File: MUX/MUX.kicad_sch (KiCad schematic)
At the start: 104 parts, among them P1 Conn_02x36_Top_Bottom, P2 DB9_Male, P3 DB9_Male, P4 DB9_Male, P5 DB9_Male

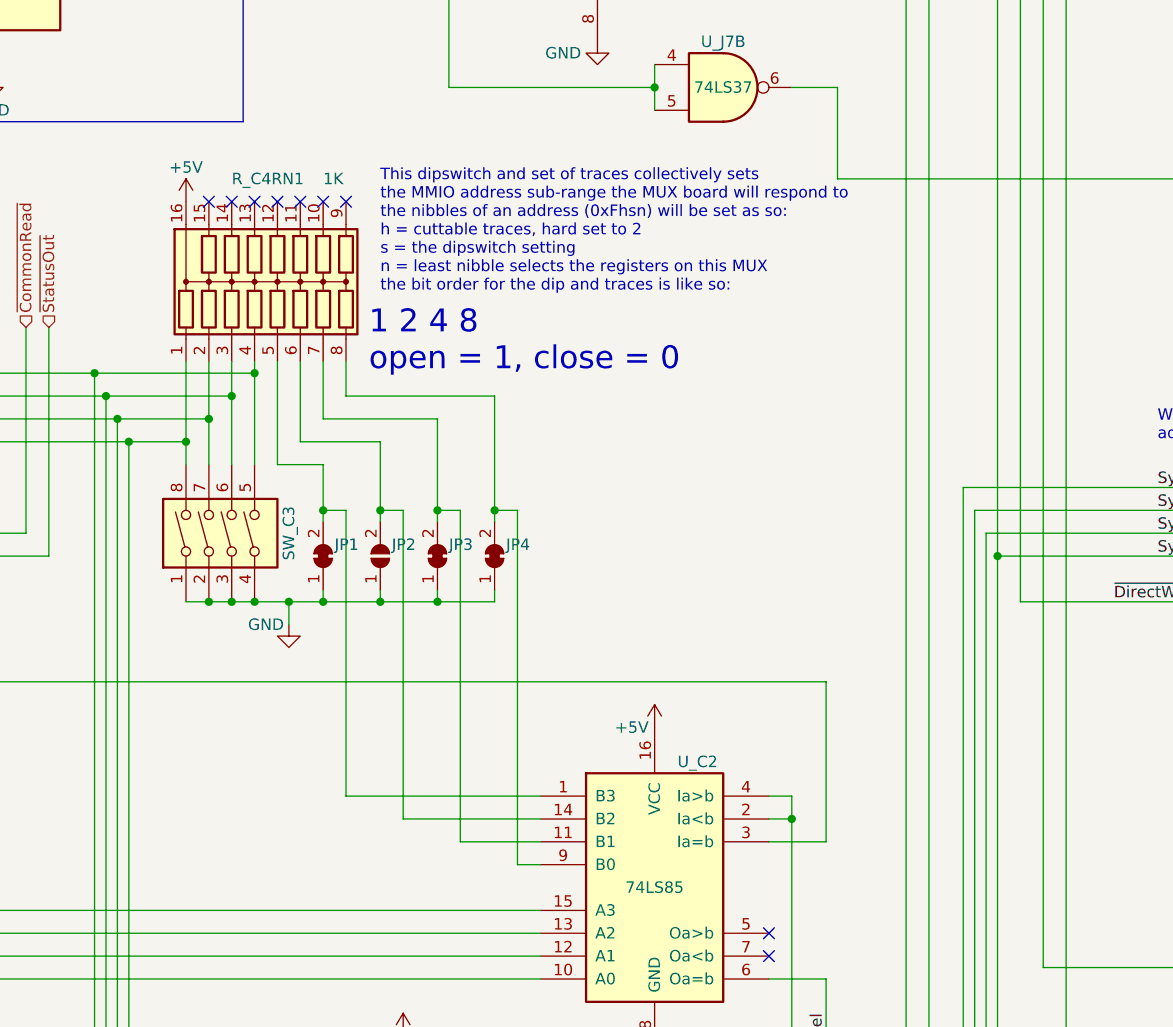
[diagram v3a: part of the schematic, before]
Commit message: Use 8-way DIP switch
Let's not bother with upper half. It's always possible to install a smaller
switch and hard-solder the upper half.
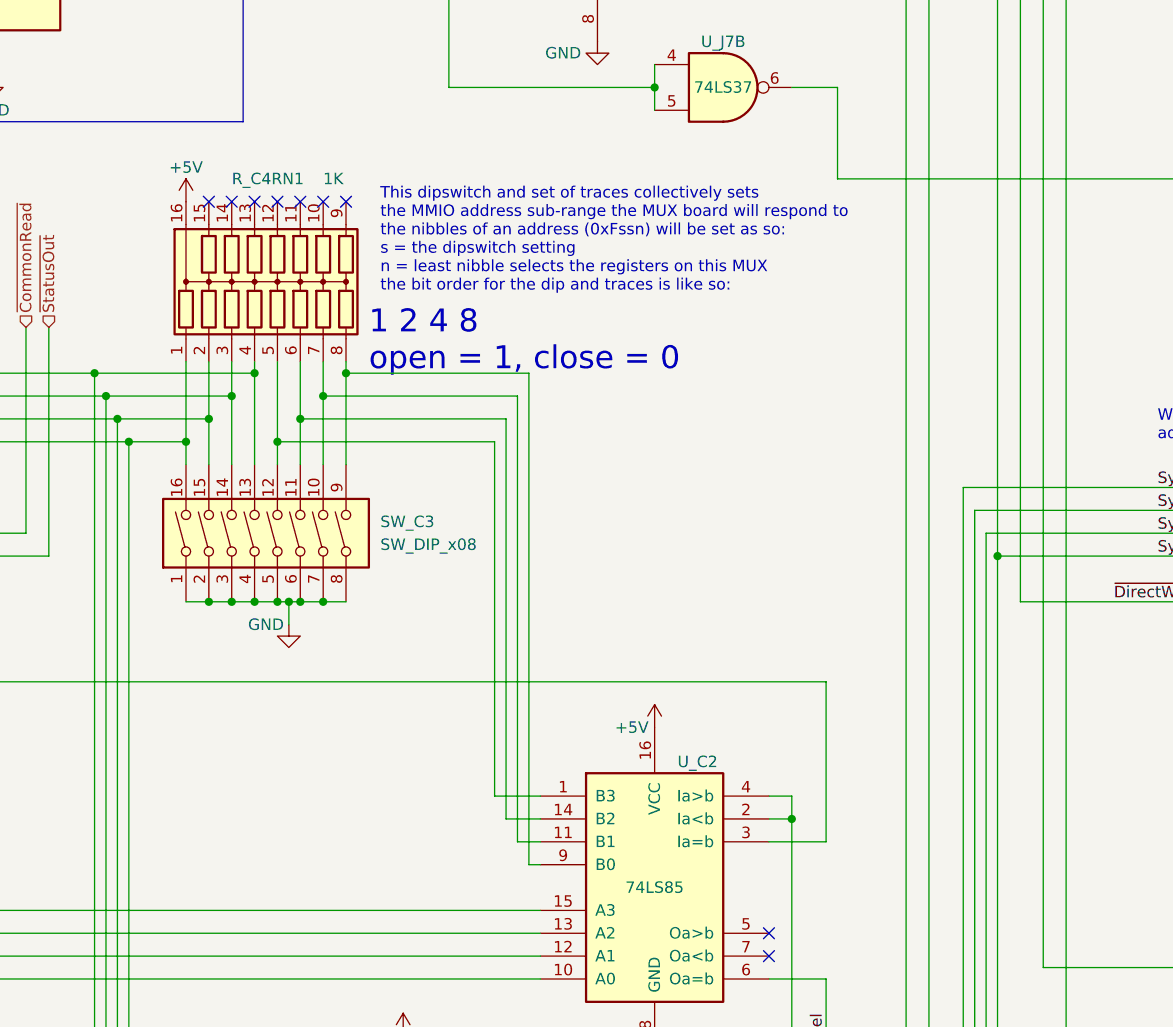
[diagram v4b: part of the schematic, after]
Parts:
- removed JP1, JP3, JP4: SolderJumper_2_Bridged, Connector_PinHeader_2.54mm:PinHeader_1x02_P2.54mm_Vertical, symbol Jumper:SolderJumper_2_Bridged
- removed JP2: SolderJumper_2_Open, Connector_PinHeader_2.54mm:PinHeader_1x02_P2.54mm_Vertical, symbol Jumper:SolderJumper_2_Open
- removed SW_C3: SW_DIP_x04, Button_Switch_THT:SW_DIP_SPSTx04_Slide_6.7x11.72mm_W7.62mm_P2.54mm_LowProfile, symbol Switch:SW_DIP_x04
- added SW_C3: SW_DIP_x08, Button_Switch_THT:SW_DIP_SPSTx08_Slide_6.7x21.88mm_W7.62mm_P2.54mm_LowProfile, symbol Switch:SW_DIP_x08
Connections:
- net GND: now also SW_C3.1, SW_C3.2, SW_C3.3, SW_C3.4, SW_C3.5, SW_C3.6, SW_C3.7, SW_C3.8
- net at R_C4RN1.4, U_C1.9 (B0), U_D4.2 (I1): now also SW_C3.13
- net at R_C4RN1.3, U_C1.11 (B1), U_D4.4 (I2): now also SW_C3.14
- net at R_C4RN1.2, U_C1.14 (B2), U_D4.6 (I3): now also SW_C3.15
- net at R_C4RN1.1, U_C1.1 (B3), U_D4.10 (I4): now also SW_C3.16
- net at R_C4RN1.7, U_C2.11 (B1): now also SW_C3.10
- net at R_C4RN1.6, U_C2.14 (B2): now also SW_C3.11
- net at R_C4RN1.5, U_C2.1 (B3): now also SW_C3.12
- net at R_C4RN1.8, U_C2.9 (B0): now also SW_C3.9
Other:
- note added: "This dipswitch and set of traces collectively sets the MMIO address sub-range the MUX board will respond to the nibbles of an address (0xFssn) will be set as so: s = the dipswitch setting n = least nibble selects the registers on this MUX the bit order for the dip and traces is like so:"
- note removed: "This dipswitch and set of traces collectively sets the MMIO address sub-range the MUX board will respond to the nibbles of an address (0xFhsn) will be set as so: h = cuttable traces, hard set to 2 s = the dipswitch setting n = least nibble selects the registers on this MUX the bit order for the dip and traces is like so:"

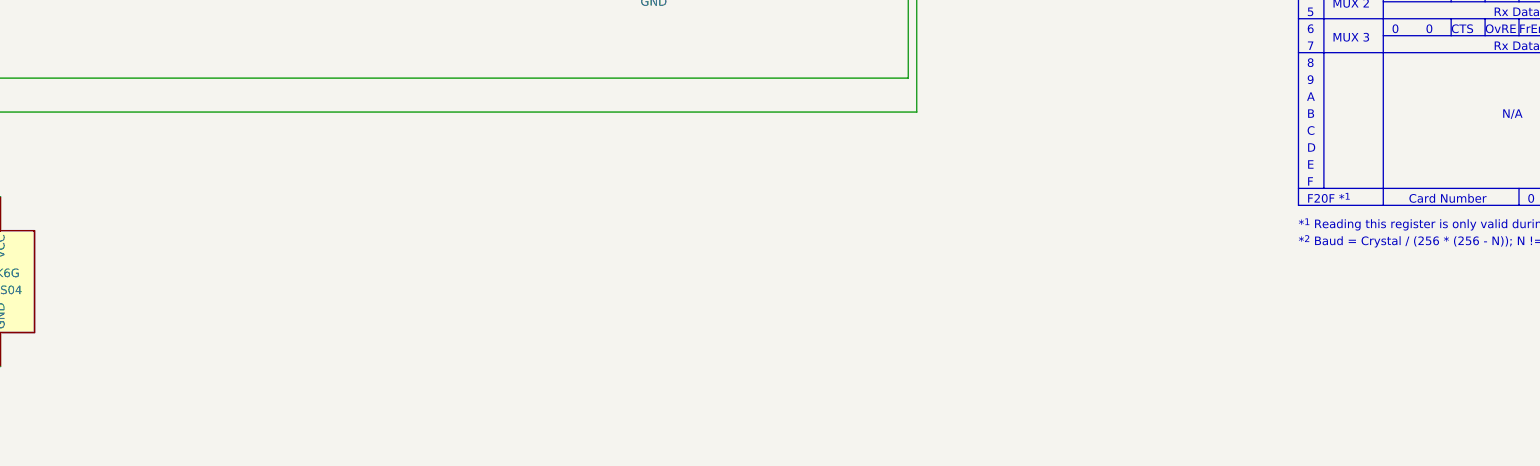
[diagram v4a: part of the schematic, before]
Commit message: MUX: Add decoupling capacitors
Based on the high-res photo. Capacitance values may not be precise, just picked
up reasonable values, like in CPU
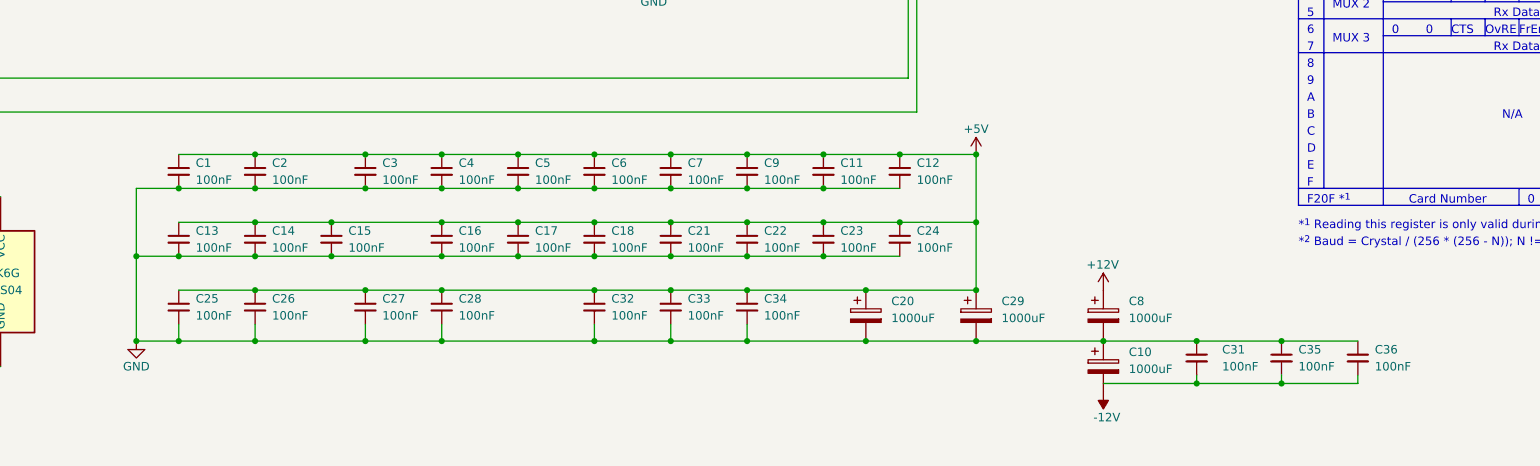
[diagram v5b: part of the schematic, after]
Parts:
- added C1, C11, C12, C13, C14, C15, C16, C17, C18, C2, C21, C22, C23, C24, C25, C26, C27, C28, C3, C31, C32, C33, C34, C35, C36, C4, C5, C6, C7, C9: 100nF, Capacitor_THT:C_Disc_D4.3mm_W1.9mm_P5.00mm, symbol Device:C_Small
- added C10, C20, C29, C8: 1000uF, Capacitor_THT:CP_Radial_D8.0mm_P3.50mm, symbol Device:C_Polarized
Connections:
- net +12V: now also C8.1
- net +5V: now also C1.1, C11.1, C12.1, C13.1, C14.1, C15.1, C16.1, C17.1, C18.1, C2.1, C20.1, C21.1, C22.1, C23.1, C24.1, C25.1, C26.1, C27.1, C28.1, C29.1, C3.1, C32.1, C33.1, C34.1, C4.1, C5.1, C6.1, C7.1, C9.1
- net -12V: now also C10.2
- net GND: now also C1.2, C10.1, C11.2, C12.2, C13.2, C14.2, C15.2, C16.2, C17.2, C18.2, C2.2, C20.2, C21.2, C22.2, C23.2, C24.2, C25.2, C26.2, C27.2, C28.2, C29.2, C3.2, C31.1, C32.2, C33.2, C34.2, C35.1, C36.1, C4.2, C5.2, C6.2, C7.2, C8.2, C9.2
- new net: C31.2, C35.2, C36.2

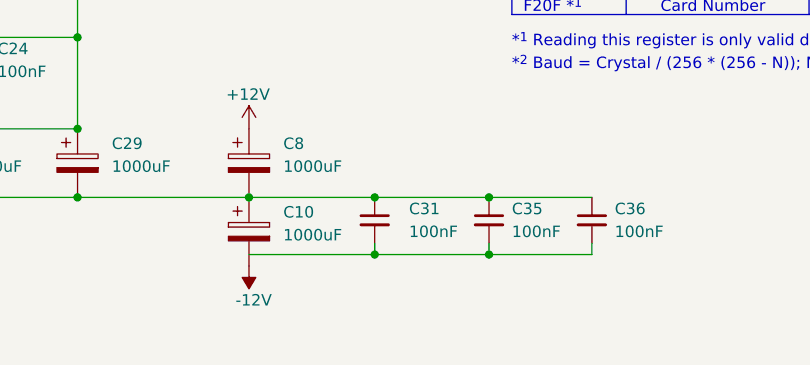
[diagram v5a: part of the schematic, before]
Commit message: MUX: Some schematic fixes
- Proper U_K5 footprint
- Fix 12V filter caps connection
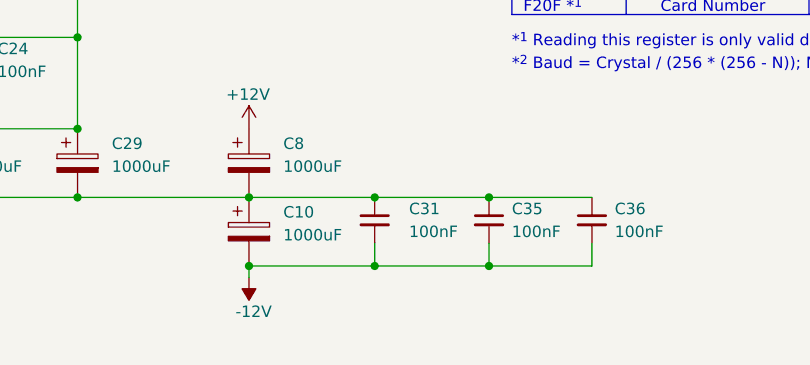
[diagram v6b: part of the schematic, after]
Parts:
- U_K5: footprint Package_DIP:DIP-16_W7.62mm -> Package_DIP:DIP-14_W7.62mm
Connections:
- net -12V: now also C31.2, C35.2, C36.2
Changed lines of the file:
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@@
   (junction (at 788.67 471.17) (diameter 0) (color 0 0 0 0)
   )
+  (junction (at 845.82 496.57) (diameter 0) (color 0 0 0 0)
+  )
   (junction (at 66.04 185.42) (diameter 0) (color 0 0 0 0)
   )
@@
   (junction (at 485.14 467.36) (diameter 0) (color 0 0 0 0)
   )
-  (junction (at 845.82 495.3) (diameter 0) (color 0 0 0 0)
-  )
   (junction (at 388.62 492.76) (diameter 0) (color 0 0 0 0)
   )
@@
   (junction (at 551.18 467.36) (diameter 0) (color 0 0 0 0)
   )
-  (junction (at 833.12 495.3) (diameter 0) (color 0 0 0 0)
-  )
   (junction (at 800.1 488.95) (diameter 0) (color 0 0 0 0)
   )
@@
   (junction (at 755.65 273.05) (diameter 0) (color 0 0 0 0)
   )
+  (junction (at 833.12 496.57) (diameter 0) (color 0 0 0 0)
+  )
   (junction (at 737.87 361.95) (diameter 0) (color 0 0 0 0)
   )
+  (junction (at 819.15 496.57) (diameter 0) (color 0 0 0 0)
+  )
   (junction (at 334.01 439.42) (diameter 0) (color 0 0 0 0)
   )
@@
     (stroke (width 0) (type default) (color 0 0 0 0))
   )
+  (wire (pts (xy 819.15 496.57) (xy 833.12 496.57))
+    (stroke (width 0) (type default) (color 0 0 0 0))
+  )
   (wire (pts (xy 651.51 133.35) (xy 671.83 133.35))
     (stroke (width 0) (type default) (color 0 0 0 0))
@@
     (stroke (width 0) (type default) (color 0 0 0 0))
   )
+  (wire (pts (xy 833.12 494.03) (xy 833.12 496.57))
+    (stroke (width 0) (type default) (color 0 0 0 0))
+  )
   (wire (pts (xy 78.74 241.3) (xy 66.04 241.3))
     (stroke (width 0) (type default) (color 0 0 0 0))
   )
+  (wire (pts (xy 819.15 497.84) (xy 819.15 496.57))
+    (stroke (width 0) (type default) (color 0 0 0 0))
+  )
   (wire (pts (xy 393.7 90.17) (xy 411.48 90.17))
     (stroke (width 0) (type default) (color 0 0 0 0))
@@
     (stroke (width 0) (type default) (color 0 0 0 0))
   )
+  (wire (pts (xy 845.82 494.03) (xy 845.82 496.57))
+    (stroke (width 0) (type default) (color 0 0 0 0))
+  )
   (wire (pts (xy 173.99 356.87) (xy 173.99 396.24))
     (stroke (width 0) (type default) (color 0 0 0 0))
@@
     (stroke (width 0) (type solid) (color 0 0 0 0))
   )
-  (wire (pts (xy 857.25 495.3) (xy 845.82 495.3))
+  (wire (pts (xy 857.25 496.57) (xy 845.82 496.57))
     (stroke (width 0) (type default) (color 0 0 0 0))
   )
@@
     (stroke (width 0) (type default) (color 0 0 0 0))
   )
-  (wire (pts (xy 845.82 495.3) (xy 845.82 494.03))
-    (stroke (width 0) (type default) (color 0 0 0 0))
-  )
   (wire (pts (xy 593.09 135.89) (xy 605.79 135.89))
     (stroke (width 0) (type default) (color 0 0 0 0))
@@
     (stroke (width 0) (type default) (color 0 0 0 0))
   )
-  (wire (pts (xy 833.12 495.3) (xy 845.82 495.3))
+  (wire (pts (xy 833.12 496.57) (xy 845.82 496.57))
     (stroke (width 0) (type default) (color 0 0 0 0))
   )
@@
     (stroke (width 0) (type default) (color 0 0 0 0))
   )
-  (wire (pts (xy 857.25 495.3) (xy 857.25 494.03))
+  (wire (pts (xy 857.25 496.57) (xy 857.25 494.03))
     (stroke (width 0) (type default) (color 0 0 0 0))
   )
@@
     (stroke (width 0) (type default) (color 0 0 0 0))
   )
-  (wire (pts (xy 819.15 495.3) (xy 833.12 495.3))
-    (stroke (width 0) (type default) (color 0 0 0 0))
-  )
   (wire (pts (xy 77.47 448.31) (xy 85.09 448.31))
     (stroke (width 0) (type default) (color 0 0 0 0))
@@
     (stroke (width 0) (type default) (color 0 0 0 0))
   )
-  (wire (pts (xy 833.12 494.03) (xy 833.12 495.3))
-    (stroke (width 0) (type default) (color 0 0 0 0))
-  )
   (wire (pts (xy 124.46 64.77) (xy 129.54 64.77))
     (stroke (width 0) (type default) (color 0 0 0 0))
@@
   (symbol (lib_id "power:GND") (at 674.37 488.95 0) (unit 1)
     (in_bom yes) (on_board yes)
-    (property "Reference" "#PWR?" (id 0) (at 674.37 495.3 0)
+    (property "Reference" "#PWR0142" (id 0) (at 674.37 495.3 0)
       (effects (font (size 1.27 1.27)) hide)
     )
@@
     (pin "9")
   )
-  (symbol (lib_id "power:-12V") (at 819.15 496.57 180) (unit 1)
+  (symbol (lib_id "power:-12V") (at 819.15 497.84 180) (unit 1)
     (in_bom yes) (on_board yes)
-    (property "Reference" "#PWR?" (id 0) (at 819.15 499.11 0)
+    (property "Reference" "#PWR0141" (id 0) (at 819.15 500.38 0)
       (effects (font (size 1.27 1.27)) hide)
     )
-    (property "Value" "-12V" (id 1) (at 821.69 500.38 0)
+    (property "Value" "-12V" (id 1) (at 821.69 501.65 0)
       (effects (font (size 1.27 1.27)) (justify left))
     )
-    (property "Footprint" "" (id 2) (at 819.15 496.57 0)
+    (property "Footprint" "" (id 2) (at 819.15 497.84 0)
       (effects (font (size 1.27 1.27)) hide)
     )
-    (property "Datasheet" "" (id 3) (at 819.15 496.57 0)
+    (property "Datasheet" "" (id 3) (at 819.15 497.84 0)
       (effects (font (size 1.27 1.27)) hide)
     )
@@
     (property "Reference" "U_K5" (id 0) (at 642.62 478.79 0))
     (property "Value" "74LS393" (id 1) (at 642.62 481.33 0))
-    (property "Footprint" "Package_DIP:DIP-16_W7.62mm" (id 2) (at 642.62 480.06 0)
+    (property "Footprint" "Package_DIP:DIP-14_W7.62mm" (id 2) (at 642.62 480.06 0)
       (effects (font (size 1.27 1.27)) hide)
     )
@@
   (symbol (lib_id "power:+12V") (at 819.15 481.33 0) (unit 1)
     (in_bom yes) (on_board yes)
-    (property "Reference" "#PWR?" (id 0) (at 819.15 485.14 0)
+    (property "Reference" "#PWR0140" (id 0) (at 819.15 485.14 0)
       (effects (font (size 1.27 1.27)) hide)
     )
@@
     (property "Reference" "U_K5" (id 0) (at 567.69 416.56 0))
     (property "Value" "74LS393" (id 1) (at 565.15 424.18 0))
-    (property "Footprint" "Package_DIP:DIP-16_W7.62mm" (id 2) (at 567.69 422.91 0)
+    (property "Footprint" "Package_DIP:DIP-14_W7.62mm" (id 2) (at 567.69 422.91 0)
       (effects (font (size 1.27 1.27)) hide)
     )
@@
     (property "Reference" "U_K5" (id 0) (at 567.69 397.51 0))
     (property "Value" "74LS393" (id 1) (at 565.15 405.13 0))
-    (property "Footprint" "Package_DIP:DIP-16_W7.62mm" (id 2) (at 567.69 403.86 0)
+    (property "Footprint" "Package_DIP:DIP-14_W7.62mm" (id 2) (at 567.69 403.86 0)
       (effects (font (size 1.27 1.27)) hide)
     )
@@
   (symbol (lib_id "power:+5V") (at 800.1 461.01 0) (unit 1)
     (in_bom yes) (on_board yes)
-    (property "Reference" "#PWR?" (id 0) (at 800.1 464.82 0)
+    (property "Reference" "#PWR0139" (id 0) (at 800.1 464.82 0)
       (effects (font (size 1.27 1.27)) hide)
     )
@@
       (reference "#PWR0138") (unit 1) (value "GND") (footprint "")
     )
-    (path "/2b72be31-dc00-46e0-a671-efb7f5c8996a"
-      (reference "#PWR?") (unit 1) (value "GND") (footprint "")
-    )
-    (path "/3340cee5-3e96-495d-8848-e872492f4f65"
-      (reference "#PWR?") (unit 1) (value "-12V") (footprint "")
+    (path "/db621c35-e7dd-427d-b02d-a8493908acb1"
+      (reference "#PWR0139") (unit 1) (value "+5V") (footprint "")
     )
     (path "/6c823c7e-2c2e-45f0-aa8e-9fd29865d7b3"
-      (reference "#PWR?") (unit 1) (value "+12V") (footprint "")
+      (reference "#PWR0140") (unit 1) (value "+12V") (footprint "")
     )
-    (path "/db621c35-e7dd-427d-b02d-a8493908acb1"
-      (reference "#PWR?") (unit 1) (value "+5V") (footprint "")
+    (path "/3340cee5-3e96-495d-8848-e872492f4f65"
+      (reference "#PWR0141") (unit 1) (value "-12V") (footprint "")
+    )
+    (path "/2b72be31-dc00-46e0-a671-efb7f5c8996a"
+      (reference "#PWR0142") (unit 1) (value "GND") (footprint "")
     )
     (path "/0b307b31-4fc8-49c4-9acc-9ae8b51ca8f2"
@@
     )
     (path "/ae78a229-7e9c-4f8d-8338-4fbfe05bedf5"
-      (reference "U_K5") (unit 1) (value "74LS393") (footprint "Package_DIP:DIP-16_W7.62mm")
+      (reference "U_K5") (unit 1) (value "74LS393") (footprint "Package_DIP:DIP-14_W7.62mm")
     )
     (path "/d731bfaa-2251-49df-ba7e-38bb6da0efa2"
-      (reference "U_K5") (unit 2) (value "74LS393") (footprint "Package_DIP:DIP-16_W7.62mm")
+      (reference "U_K5") (unit 2) (value "74LS393") (footprint "Package_DIP:DIP-14_W7.62mm")
     )
     (path "/40c27bbe-f856-4d27-82db-12764df5dfbb"
-      (reference "U_K5") (unit 3) (value "74LS393") (footprint "Package_DIP:DIP-16_W7.62mm")
+      (reference "U_K5") (unit 3) (value "74LS393") (footprint "Package_DIP:DIP-14_W7.62mm")
     )
     (path "/0f480fe1-b1a3-4ae4-8a93-10d2d45319ce"
